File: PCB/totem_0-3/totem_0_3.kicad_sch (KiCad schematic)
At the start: 96 parts, among them J1 MJ-4PP-9, J2 MJ-4PP-9, J3 Conn_01x03_Socket, J4 Conn_01x03_Socket, J5 Conn_01x12_Socket, J6 Conn_01x12_Socket, U1 xiao-ble, U2 xiao-ble, U3 74HC595, U4 74HC595

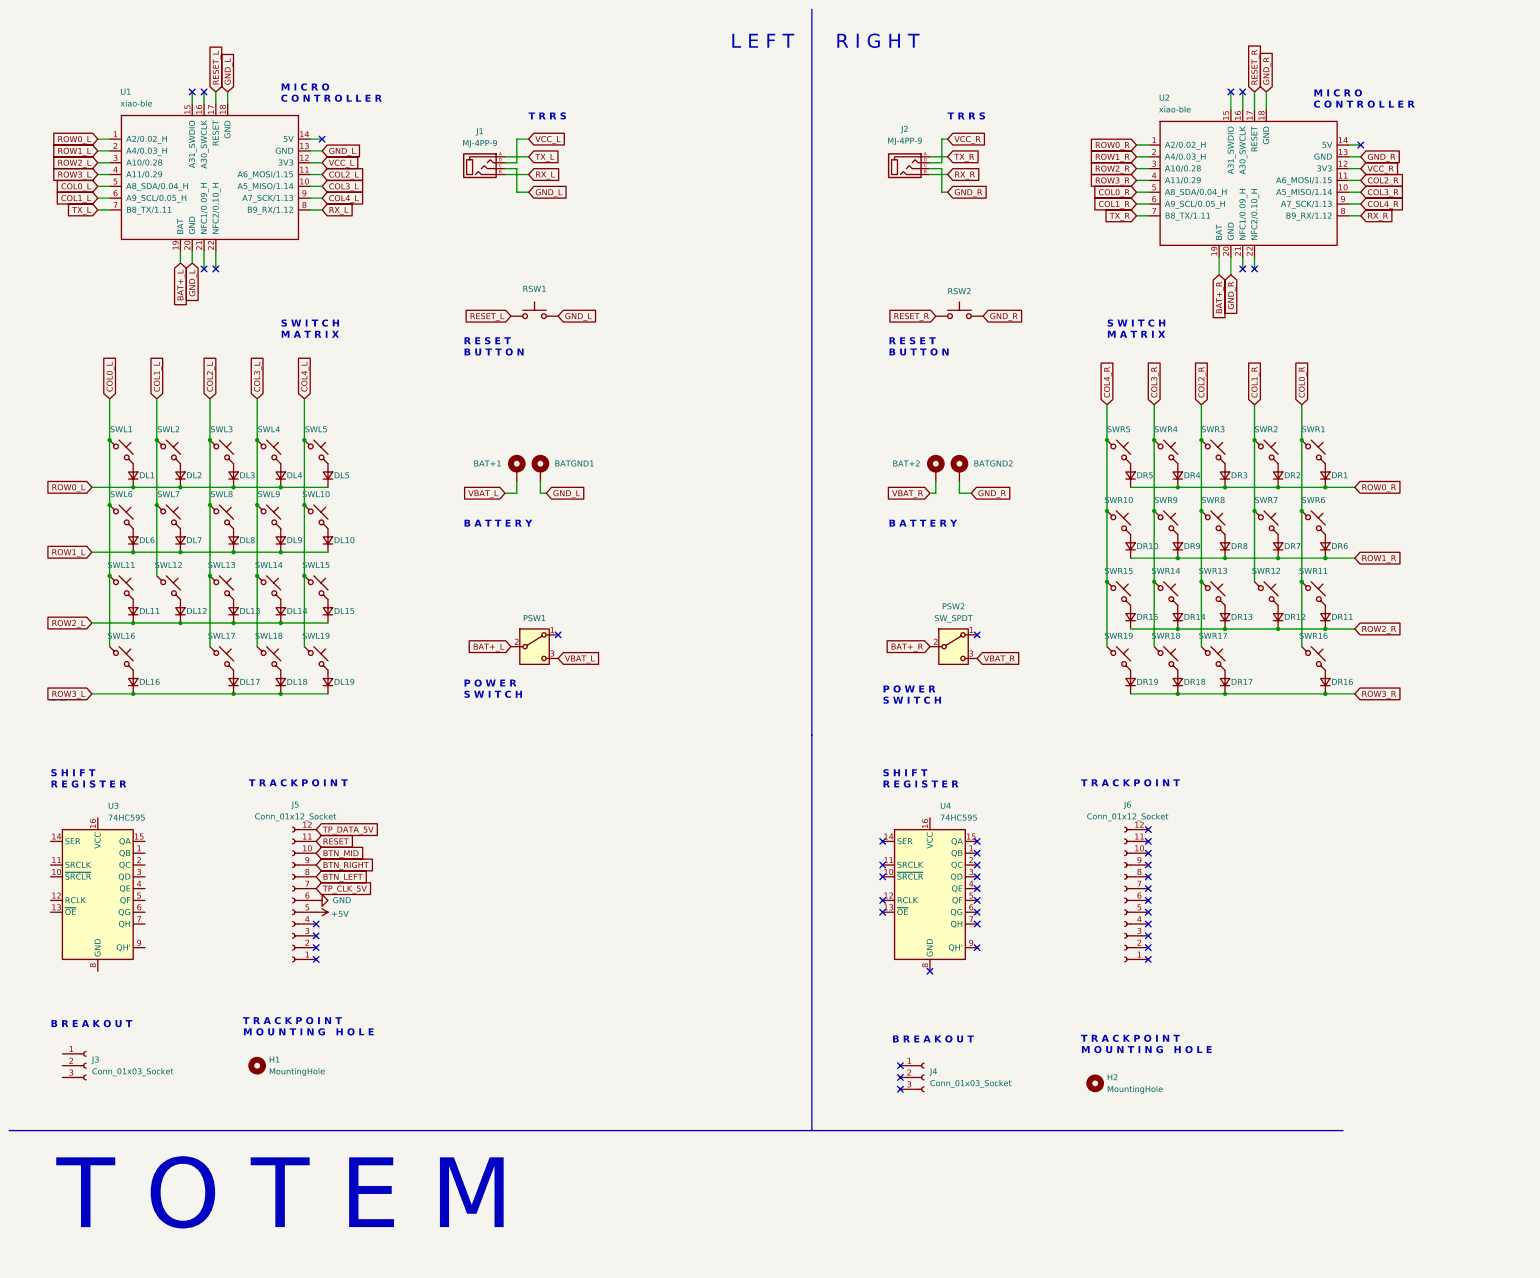
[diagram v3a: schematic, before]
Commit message: pcb: fix up references
Signed-off-by: Anant Thazhemadam <anant.thazhemadam@gmail.com>
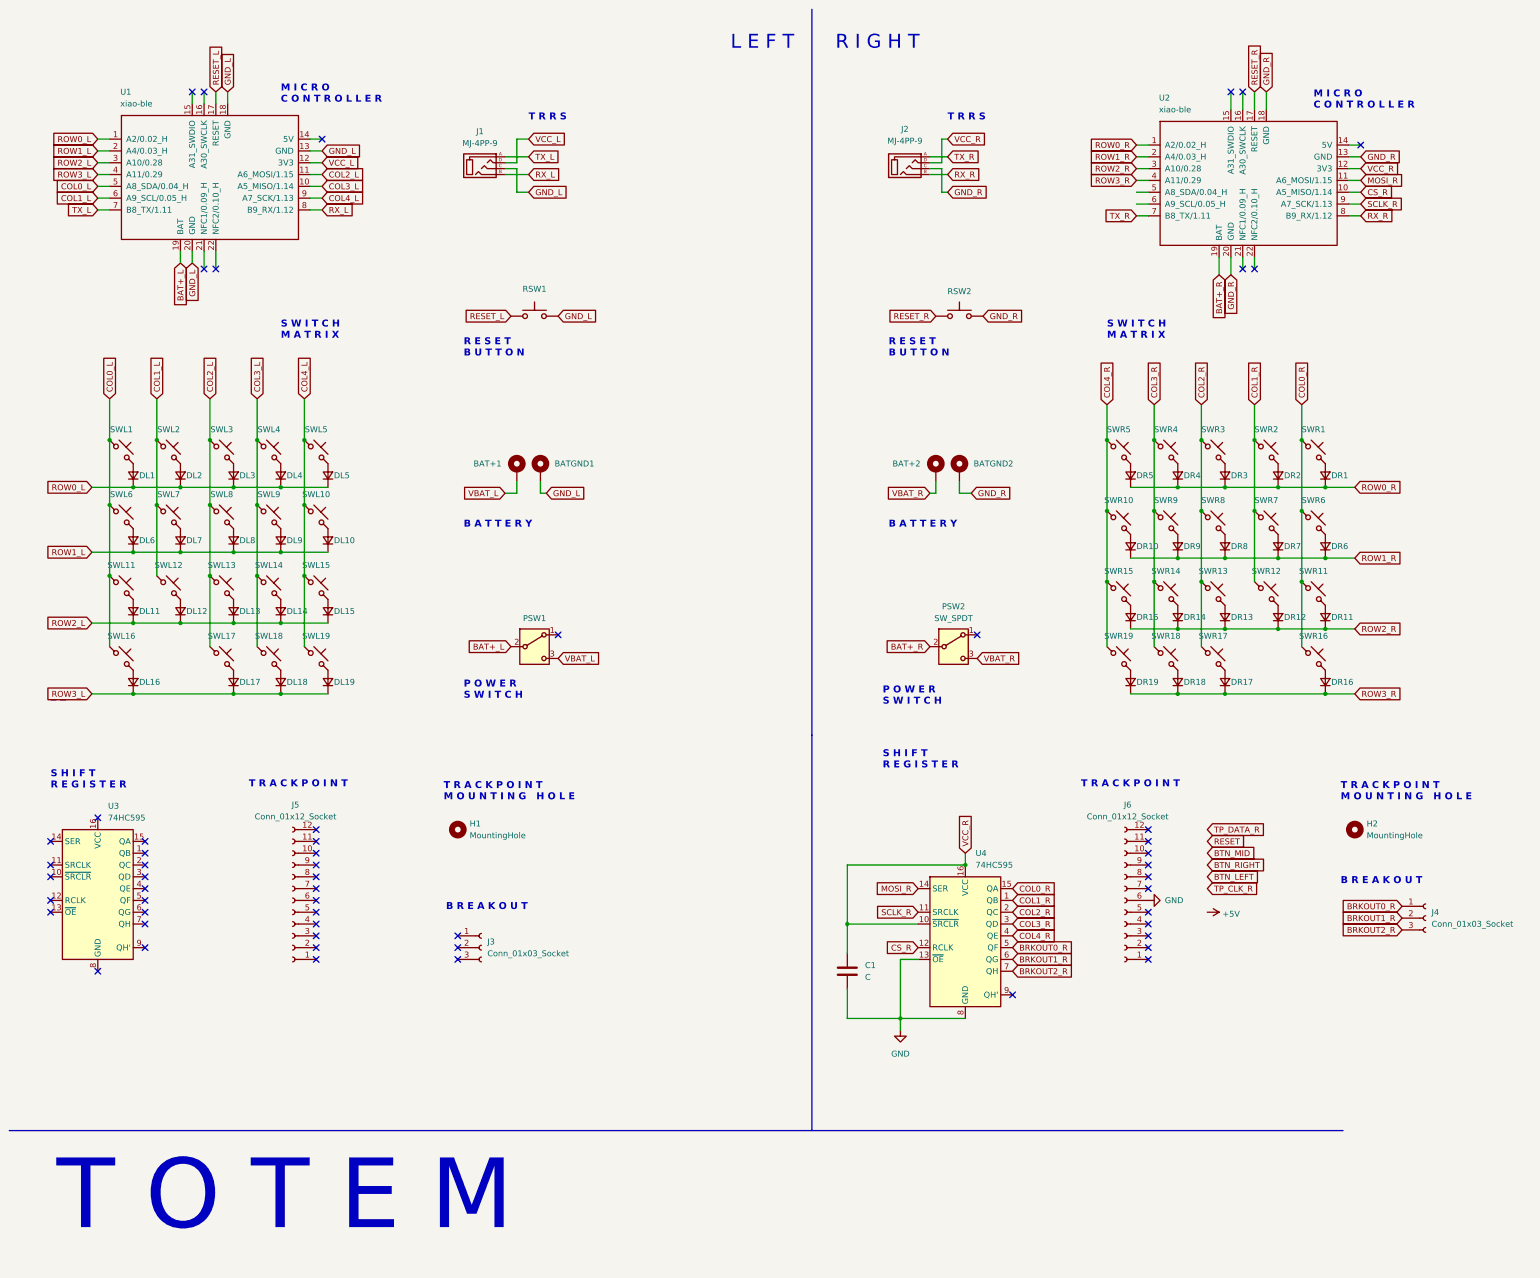
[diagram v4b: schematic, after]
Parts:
- added C1: C, Capacitor_SMD:C_0805_2012Metric_Pad1.18x1.45mm_HandSolder, symbol Device:C
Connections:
- net +5V: no longer J5.5 (Pin_5)
- net BTN_LEFT: no longer J5.8 (Pin_8)
- net BTN_MID: no longer J5.10 (Pin_10)
- net BTN_RIGHT: no longer J5.9 (Pin_9)
- net COL0_R: now also U4.15 (QA); no longer U2.5 (A8_SDA/0.04_H)
- net COL1_R: now also U4.1 (QB); no longer U2.6 (A9_SCL/0.05_H)
- net COL2_R: now also U4.2 (QC); no longer U2.11 (A6_MOSI/1.15)
- net COL3_R: now also U4.3 (QD); no longer U2.10 (A5_MISO/1.14)
- net COL4_R: now also U4.4 (QE); no longer U2.9 (A7_SCK/1.13)
- net GND: now also J6.6 (Pin_6), U4.13 (~{OE}), U4.8 (GND), C1.2; no longer J5.6 (Pin_6)
- net RESET: no longer J5.11 (Pin_11)
- net VCC_R: now also U4.10 (~{SRCLR}), U4.16 (VCC), C1.1
- net SCLK_R: now reaches U4.11 (SRCLK)
- net SCLK_R: now also U2.9 (A7_SCK/1.13)
- net CS_R: now reaches U4.12 (RCLK)
- net CS_R: now also U2.10 (A5_MISO/1.14)
- net MOSI_R: now reaches U4.14 (SER)
- net MOSI_R: now also U2.11 (A6_MOSI/1.15)
- net BRKOUT0_R: now reaches U4.5 (QF)
- net BRKOUT0_R: now also J4.1 (Pin_1)
- net BRKOUT1_R: now reaches U4.6 (QG)
- net BRKOUT1_R: now also J4.2 (Pin_2)
- net BRKOUT2_R: now reaches U4.7 (QH)
- net BRKOUT2_R: now also J4.3 (Pin_3)
- net TP_CLK_5V: no longer names the net of J5.7 (Pin_7)
- net TP_DATA_5V: no longer names the net of J5.12 (Pin_12)
- no-connect marks 46 -> 55
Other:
- moved on the sheet: U4

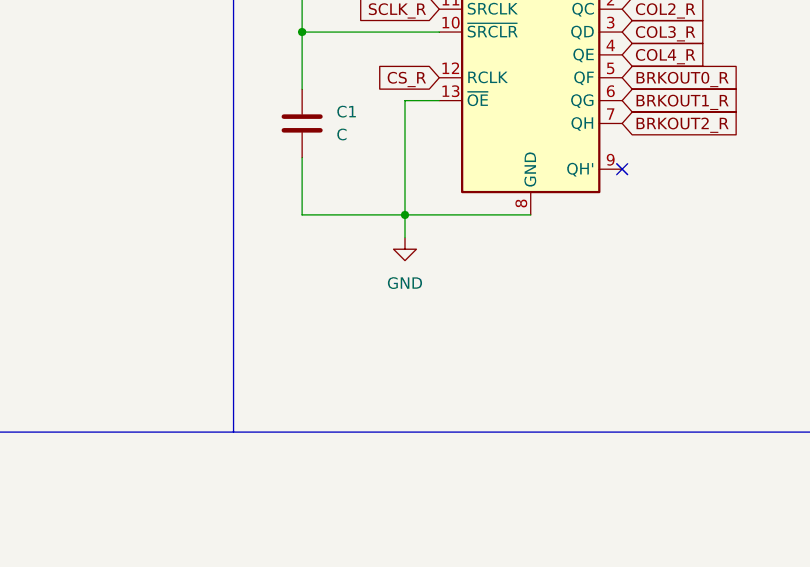
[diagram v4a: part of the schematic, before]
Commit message: pcb: wire up shift register
Signed-off-by: Anant Thazhemadam <anant.thazhemadam@gmail.com>
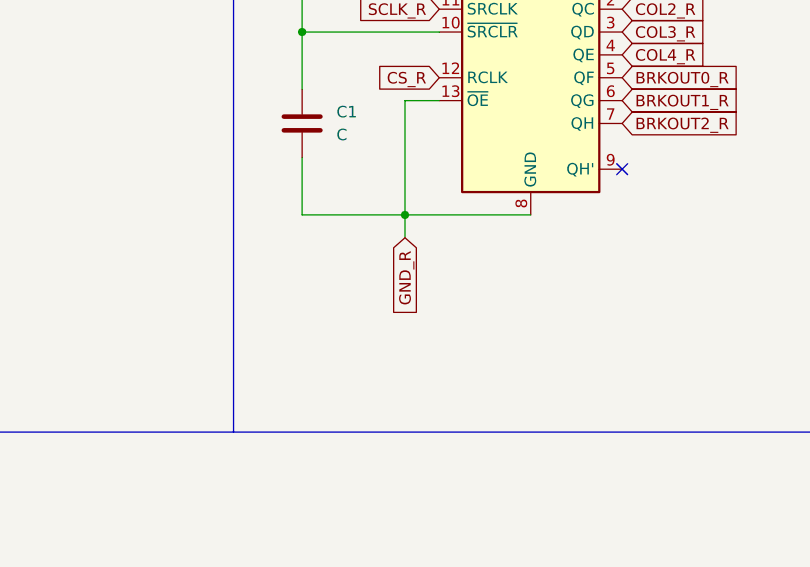
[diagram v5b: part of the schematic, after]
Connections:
- net GND: no longer C1.2, U4.13 (~{OE}), U4.8 (GND)
- net GND_R: now also C1.2, U4.13 (~{OE}), U4.8 (GND)
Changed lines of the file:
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@@
 		)
 	)
+	(global_label "GND_R"
+		(shape input)
+		(at 204.47 232.41 270)
+		(fields_autoplaced yes)
+		(effects
+			(font
+				(size 1.27 1.27)
+			)
+			(justify right)
+		)
+		(property "Intersheetrefs" "${INTERSHEET_REFS}"
+			(at 204.47 241.5033 90)
+			(effects
+				(font
+					(size 1.27 1.27)
+				)
+				(justify right)
+				(hide yes)
+			)
+		)
+	)
 	(global_label "COL4_R"
 		(shape input)
@@
 					(unit 1)
 				)
-			)
-		)
-	)
-	(symbol
-		(lib_id "power:GND")
-		(at 204.47 232.41 0)
-		(unit 1)
-		(exclude_from_sim no)
-		(in_bom yes)
-		(on_board yes)
-		(dnp no)
-		(fields_autoplaced yes)
-		(property "Reference" "#PWR05"
-			(at 204.47 238.76 0)
-			(effects
-				(font
-					(size 1.27 1.27)
-				)
-				(hide yes)
-			)
-		)
-		(property "Value" "GND"
-			(at 204.47 237.49 0)
-			(effects
-				(font
-					(size 1.27 1.27)
-				)
-			)
-		)
-		(property "Footprint" ""
-			(at 204.47 232.41 0)
-			(effects
-				(font
-					(size 1.27 1.27)
-				)
-				(hide yes)
-			)
-		)
-		(property "Datasheet" ""
-			(at 204.47 232.41 0)
-			(effects
-				(font
-					(size 1.27 1.27)
-				)
-				(hide yes)
-			)
-		)
-		(property "Description" "Power symbol creates a global label with name \"GND\" , ground"
-			(at 204.47 232.41 0)
-			(effects
-				(font
-					(size 1.27 1.27)
-				)
-				(hide yes)
-			)
-		)
-		(pin "1"
-		)
-		(instances
-			(project "totem_0_3"
-				(path "/4d1e609f-5432-4afb-8ee7-7d2d9aaaee48"
-					(reference "#PWR05")
-					(unit 1)
-				)
